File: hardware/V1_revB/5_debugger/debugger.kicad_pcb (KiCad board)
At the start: 2 copper layers, 34.6 x 49.8 mm, 29 parts, among them J10 Conn_ARM_JTAG_SWD_20, J9 

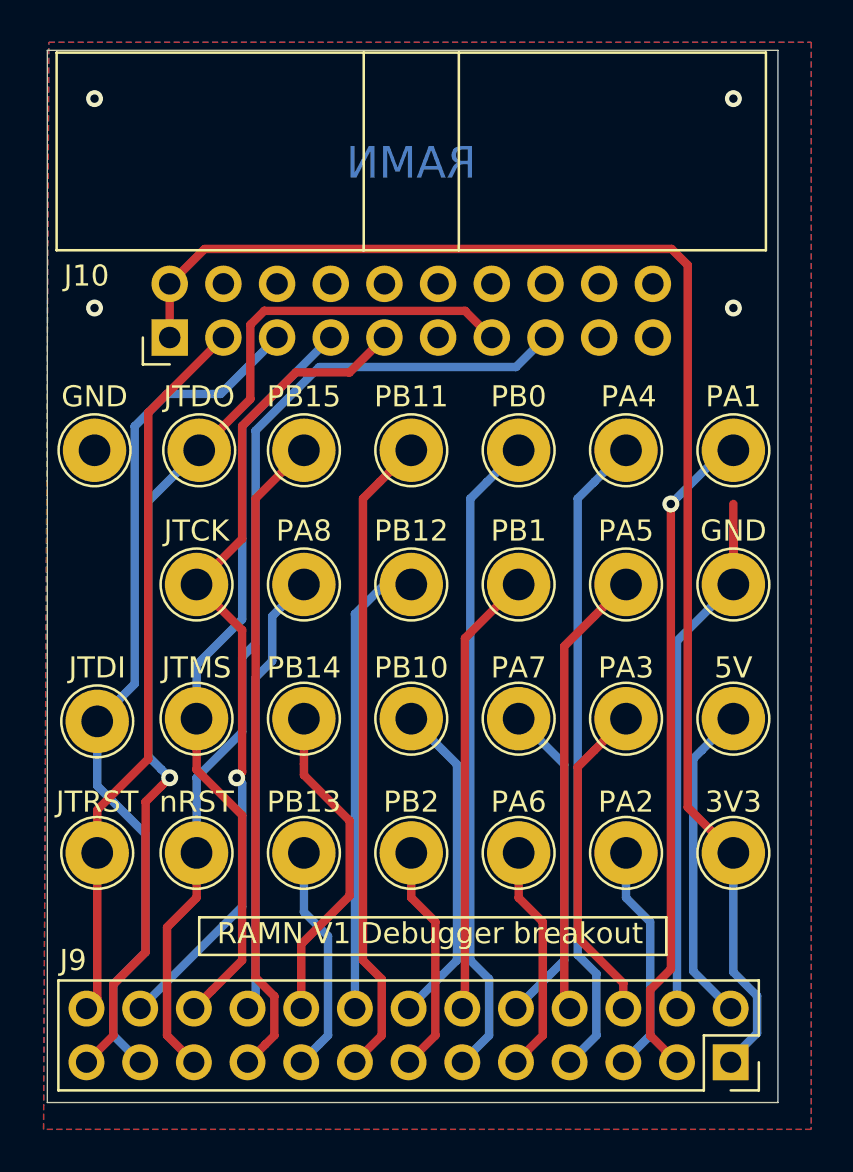
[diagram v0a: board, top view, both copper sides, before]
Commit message: feat: debugger test points changed
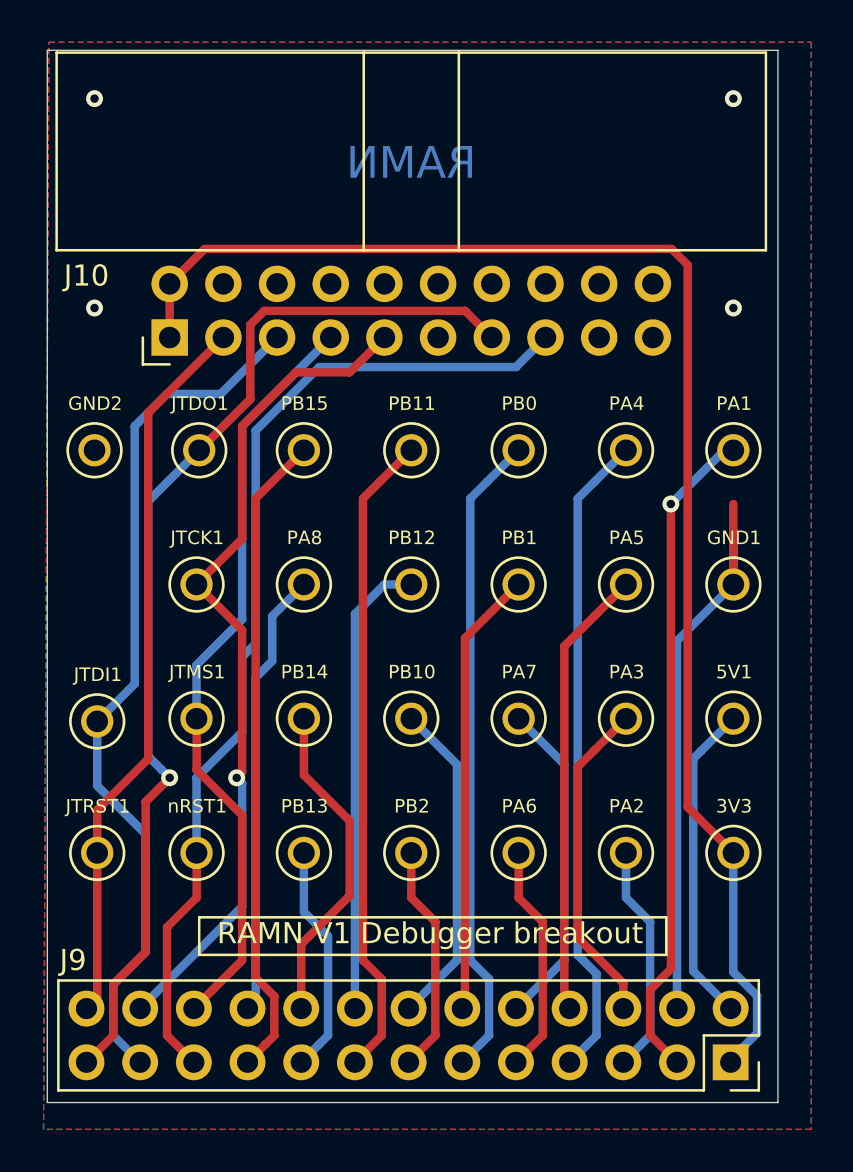
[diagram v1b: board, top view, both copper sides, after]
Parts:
- 3V3, PA1, PA2, PA3, PA4, PA5, PA6, PA7, PA8, PB0, PB1, PB10, PB11, PB12, PB13, PB14, PB15, PB2: footprint TestPoint:TestPoint_Loop_D2.54mm_Drill1.5mm_Beaded -> Global_Library:KEYSTONE_5002
- 5V1: renamed from 5V; footprint TestPoint:TestPoint_Loop_D2.54mm_Drill1.5mm_Beaded -> Global_Library:KEYSTONE_5002
- GND1, GND2: renamed from GND; footprint TestPoint:TestPoint_Loop_D2.54mm_Drill1.5mm_Beaded -> Global_Library:KEYSTONE_5002
- J9: value (none) -> ~
- JTCK1: renamed from JTCK; footprint TestPoint:TestPoint_Loop_D2.54mm_Drill1.5mm_Beaded -> Global_Library:KEYSTONE_5002
- JTDI1: renamed from JTDI; footprint TestPoint:TestPoint_Loop_D2.54mm_Drill1.5mm_Beaded -> Global_Library:KEYSTONE_5002
- JTDO1: renamed from JTDO; footprint TestPoint:TestPoint_Loop_D2.54mm_Drill1.5mm_Beaded -> Global_Library:KEYSTONE_5002
- JTMS1: renamed from JTMS; footprint TestPoint:TestPoint_Loop_D2.54mm_Drill1.5mm_Beaded -> Global_Library:KEYSTONE_5002
- JTRST1: renamed from JTRST; footprint TestPoint:TestPoint_Loop_D2.54mm_Drill1.5mm_Beaded -> Global_Library:KEYSTONE_5002
- nRST1: renamed from nRST; footprint TestPoint:TestPoint_Loop_D2.54mm_Drill1.5mm_Beaded -> Global_Library:KEYSTONE_5002
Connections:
- J10 pad 11: Net-(J10-Pad11) -> unconnected-(J10-RTCK-Pad11)
- J10 pad 17: Net-(J10-Pad17) -> unconnected-(J10-DBGRQ/NC-Pad17)
- J10 pad 19: Net-(J10-Pad19) -> unconnected-(J10-DBGACK/NC-Pad19)
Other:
- net class Default removed
